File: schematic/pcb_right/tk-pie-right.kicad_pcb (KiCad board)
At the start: 2 copper layers, 150 x 77.5 mm, 35 parts, among them IC1 PCA9539PW,118, J1 NiceView, J2 Battery Connector, U3 SN74LVC1T45DCK

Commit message: Save Ferris
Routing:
- net +5V: track 494.6 -> 490.6 mm, vias 47 -> 45
- net Net-(E3-Pin_1): track 21.5 -> 21.7 mm, vias 0 -> 2
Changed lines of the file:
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@@
 			(xy 96.522284 92.276211) (xy 96.526544 92.29515) (xy 96.531557 92.314169) (xy 96.537324 92.33327)
 			(xy 96.543844 92.35246) (xy 96.55112 92.371739) (xy 96.559148 92.391111) (xy 96.567932 92.410581)
-			(xy 96.587762 92.449827) (xy 96.610607 92.489504) (xy 96.610607 92.489504) (xy 96.628756 92.517845)
-			(xy 96.64862 92.546306) (xy 96.669998 92.574691) (xy 96.692681 92.602813) (xy 96.716468 92.630473)
-			(xy 96.741152 92.657481) (xy 96.766529 92.683644) (xy 96.792395 92.708769) (xy 96.818541 92.732662)
-			(xy 96.844768 92.75513) (xy 96.87087 92.775982) (xy 96.896639 92.795024) (xy 96.921872 92.812061)
-			(xy 96.946366 92.826904) (xy 96.969914 92.839355) (xy 96.992312 92.849226) (xy 97.003643 92.853415)
-			(xy 97.015692 92.857404) (xy 97.028374 92.861183) (xy 97.041608 92.864733) (xy 97.055307 92.868048)
-			(xy 97.06939 92.871107) (xy 97.083773 92.873901) (xy 97.09837 92.876414) (xy 97.113099 92.878634)
-			(xy 97.127877 92.880549) (xy 97.14262 92.882141) (xy 97.157243 92.883401) (xy 97.171663 92.884313)
-			(xy 97.185796 92.884863) (xy 97.199561 92.885041) (xy 97.212869 92.88483) (xy 97.218868 92.88452)
-			(xy 97.225592 92.883953) (xy 97.241046 92.88207) (xy 97.258908 92.879248) (xy 97.278855 92.875549)
-			(xy 97.300562 92.871036) (xy 97.323707 92.865774) (xy 97.347966 92.859825) (xy 97.373015 92.853256)
-			(xy 97.404738 92.844479) (xy 97.43221 92.836397) (xy 97.456496 92.828612) (xy 97.478662 92.820724)
-			(xy 97.49977 92.812333) (xy 97.520886 92.803036) (xy 97.543074 92.792435) (xy 97.567396 92.780129)
-			(xy 97.607879 92.758394) (xy 97.648636 92.734868) (xy 97.689467 92.709687) (xy 97.73018 92.682981)
-			(xy 97.770573 92.654888) (xy 97.810452 92.625538) (xy 97.849618 92.595063) (xy 97.887874 92.5636)
-			(xy 97.912491 92.542576) (xy 97.932105 92.525158) (xy 97.940339 92.517441) (xy 97.947685 92.510198)
-			(xy 97.954263 92.503281) (xy 97.960196 92.49655) (xy 97.965606 92.48986) (xy 97.970611 92.483069)
-			(xy 97.975336 92.476032) (xy 97.979898 92.468608) (xy 97.984422 92.460651) (xy 97.989026 92.452019)
-			(xy 97.998962 92.432156) (xy 98.006663 92.415786) (xy 98.014105 92.398829) (xy 98.021266 92.38137)
-			(xy 98.028123 92.363495) (xy 98.034651 92.345284) (xy 98.040826 92.32683) (xy 98.046625 92.308214)
-			(xy 98.052025 92.289522) (xy 98.057001 92.270839) (xy 98.061531 92.252253) (xy 98.065589 92.233847)
-			(xy 98.069153 92.215705) (xy 98.072198 92.197915) (xy 98.074701 92.180563) (xy 98.07664 92.163732)
-			(xy 98.077989 92.147508) (xy 98.079304 92.125085) (xy 98.079668 92.115331) (xy 98.079789 92.106249)
-			(xy 98.079631 92.097618) (xy 98.079154 92.089211) (xy 98.078327 92.080804) (xy 98.077112 92.072171)
-			(xy 98.07547 92.06309) (xy 98.07337 92.053336) (xy 98.070772 92.042685) (xy 98.06764 92.030911) (xy 98.063938 92.017791)
+			(xy 96.587762 92.449827) (xy 96.610607 92.489504) (xy 96.628756 92.517845) (xy 96.64862 92.546306)
+			(xy 96.669998 92.574691) (xy 96.692681 92.602813) (xy 96.716468 92.630473) (xy 96.741152 92.657481)
+			(xy 96.766529 92.683644) (xy 96.792395 92.708769) (xy 96.818541 92.732662) (xy 96.844768 92.75513)
+			(xy 96.87087 92.775982) (xy 96.896639 92.795024) (xy 96.921872 92.812061) (xy 96.946366 92.826904)
+			(xy 96.969914 92.839355) (xy 96.992312 92.849226) (xy 97.003643 92.853415) (xy 97.015692 92.857404)
+			(xy 97.028374 92.861183) (xy 97.041608 92.864733) (xy 97.055307 92.868048) (xy 97.06939 92.871107)
+			(xy 97.083773 92.873901) (xy 97.09837 92.876414) (xy 97.113099 92.878634) (xy 97.127877 92.880549)
+			(xy 97.14262 92.882141) (xy 97.157243 92.883401) (xy 97.171663 92.884313) (xy 97.185796 92.884863)
+			(xy 97.199561 92.885041) (xy 97.212869 92.88483) (xy 97.218868 92.88452) (xy 97.225592 92.883953)
+			(xy 97.241046 92.88207) (xy 97.258908 92.879248) (xy 97.278855 92.875549) (xy 97.300562 92.871036)
+			(xy 97.323707 92.865774) (xy 97.347966 92.859825) (xy 97.373015 92.853256) (xy 97.404738 92.844479)
+			(xy 97.43221 92.836397) (xy 97.456496 92.828612) (xy 97.478662 92.820724) (xy 97.49977 92.812333)
+			(xy 97.520886 92.803036) (xy 97.543074 92.792435) (xy 97.567396 92.780129) (xy 97.607879 92.758394)
+			(xy 97.648636 92.734868) (xy 97.689467 92.709687) (xy 97.73018 92.682981) (xy 97.770573 92.654888)
+			(xy 97.810452 92.625538) (xy 97.849618 92.595063) (xy 97.887874 92.5636) (xy 97.912491 92.542576)
+			(xy 97.932105 92.525158) (xy 97.940339 92.517441) (xy 97.947685 92.510198) (xy 97.954263 92.503281)
+			(xy 97.960196 92.49655) (xy 97.965606 92.48986) (xy 97.970611 92.483069) (xy 97.975336 92.476032)
+			(xy 97.979898 92.468608) (xy 97.984422 92.460651) (xy 97.989026 92.452019) (xy 97.998962 92.432156)
+			(xy 98.006663 92.415786) (xy 98.014105 92.398829) (xy 98.021266 92.38137) (xy 98.028123 92.363495)
+			(xy 98.034651 92.345284) (xy 98.040826 92.32683) (xy 98.046625 92.308214) (xy 98.052025 92.289522)
+			(xy 98.057001 92.270839) (xy 98.061531 92.252253) (xy 98.065589 92.233847) (xy 98.069153 92.215705)
+			(xy 98.072198 92.197915) (xy 98.074701 92.180563) (xy 98.07664 92.163732) (xy 98.077989 92.147508)
+			(xy 98.079304 92.125085) (xy 98.079668 92.115331) (xy 98.079789 92.106249) (xy 98.079631 92.097618)
+			(xy 98.079154 92.089211) (xy 98.078327 92.080804) (xy 98.077112 92.072171) (xy 98.07547 92.06309)
+			(xy 98.07337 92.053336) (xy 98.070772 92.042685) (xy 98.06764 92.030911) (xy 98.063938 92.017791)
 			(xy 98.05963 92.0031) (xy 98.049056 91.968107) (xy 98.038972 91.935534) (xy 98.030296 91.908836)
 			(xy 98.022526 91.886858) (xy 98.018826 91.877274) (xy 98.015165 91.868434) (xy 98.011483 91.860194)
@@
 	)
 	(segment
-		(start 99.137347 92.962653)
-		(end 100.4 91.7)
-		(width 0.25)
-		(layer "F.Cu")
-		(net 3)
-	)
-	(segment
 		(start 92.312653 85.612653)
 		(end 91 84.3)
@@
 	)
 	(segment
-		(start 99.137347 93.062653)
-		(end 99.137347 92.962653)
-		(width 0.25)
-		(layer "F.Cu")
-		(net 3)
-	)
-	(segment
 		(start 64.187347 41.487347)
 		(end 65.062653 42.362653)
@@
 	)
 	(via
-		(at 100.4 91.7)
-		(size 0.8)
-		(drill 0.4)
-		(layers "F.Cu" "B.Cu")
-		(net 3)
-	)
-	(via
 		(at 80.375 42.4)
 		(size 0.8)
@@
 		(net 3)
 	)
-	(via
-		(at 99.137347 93.062653)
-		(size 0.8)
-		(drill 0.4)
-		(layers "F.Cu" "B.Cu")
-		(net 3)
-	)
 	(segment
 		(start 66.5 42.362653)
@@
 	)
 	(segment
+		(start 99.898905 92.301095)
+		(end 99.898905 92.161095)
+		(width 0.25)
+		(layer "B.Cu")
+		(net 3)
+	)
+	(segment
 		(start 151.0755 83.849)
 		(end 131.7 83.849)
@@
 	)
 	(segment
-		(start 102.9 93.88)
-		(end 101.61781 93.88)
-		(width 0.25)
-		(layer "B.Cu")
-		(net 3)
-	)
-	(segment
 		(start 50.78 58.88)
 		(end 51.45 58.88)
@@
 	)
 	(segment
-		(start 100.4 91.7)
-		(end 102.58 93.88)
-		(width 0.25)
-		(layer "B.Cu")
-		(net 3)
-	)
-	(segment
 		(start 118.475 61)
 		(end 103.5 61)
@@
 	)
 	(segment
+		(start 98.7 93.5)
+		(end 99.898905 92.301095)
+		(width 0.25)
+		(layer "B.Cu")
+		(net 3)
+	)
+	(segment
 		(start 146.45 61.88)
 		(end 142.575 61.88)
@@
 	)
 	(segment
-		(start 101.61781 93.88)
-		(end 100.068905 92.331095)
-		(width 0.25)
-		(layer "B.Cu")
-		(net 3)
-	)
-	(segment
 		(start 29.15 39)
 		(end 29.9 39)
@@
 	)
 	(segment
+		(start 99.898905 92.161095)
+		(end 101.61781 93.88)
+		(width 0.25)
+		(layer "B.Cu")
+		(net 3)
+	)
+	(segment
 		(start 127.45 61.88)
 		(end 125.432306 61.88)
@@
 	)
 	(segment
-		(start 102.58 93.88)
-		(end 102.9 93.88)
-		(width 0.25)
-		(layer "B.Cu")
-		(net 3)
-	)
-	(segment
 		(start 93.350463 85.612653)
 		(end 92.312653 85.612653)
@@
 	)
 	(segment
-		(start 98.7 93.5)
-		(end 99.137347 93.062653)
-		(width 0.25)
-		(layer "B.Cu")
-		(net 3)
-	)
-	(segment
 		(start 146.5 61.3)
 		(end 146.5 61.83)
@@
 	)
 	(segment
-		(start 108.45 93.88)
-		(end 102.9 93.88)
-		(width 0.25)
-		(layer "B.Cu")
-		(net 3)
-	)
-	(segment
 		(start 116.137347 78.725)
 		(end 108.025 78.725)
@@
 	)
 	(segment
+		(start 101.61781 93.88)
+		(end 108.45 93.88)
+		(width 0.25)
+		(layer "B.Cu")
+		(net 3)
+	)
+	(segment
 		(start 63.78 41.38)
 		(end 63.887347 41.487347)
@@
 	)
 	(segment
-		(start 100.068905 92.331095)
+		(start 99.898905 92.161095)
 		(end 93.350463 85.612653)
 		(width 0.25)
@@
 	)
 	(segment
-		(start 98.35 91.25)
-		(end 88.65 91.25)
+		(start 93.93 93.055)
+		(end 95.1 94.225)
+		(width 0.25)
+		(layer "F.Cu")
+		(net 36)
+	)
+	(segment
+		(start 93.93 92.775)
+		(end 93.93 93.055)
+		(width 0.25)
+		(layer "F.Cu")
+		(net 36)
+	)
+	(via
+		(at 93.93 92.775)
+		(size 0.8)
+		(drill 0.4)
+		(layers "F.Cu" "B.Cu")
+		(net 36)
+	)
+	(via
+		(at 95.1 94.225)
+		(size 0.8)
+		(drill 0.4)
+		(layers "F.Cu" "B.Cu")
+		(net 36)
+	)
+	(segment
+		(start 96.255 95.38)
+		(end 108.45 95.38)
+		(width 0.25)
+		(layer "B.Cu")
+		(net 36)
+	)
+	(segment
+		(start 95.1 94.225)
+		(end 96.255 95.38)
 		(width 0.25)
 		(layer "B.Cu")
@@
 	)
 	(segment
-		(start 102.48 95.38)
-		(end 98.35 91.25)
+		(start 88.65 91.25)
+		(end 92.405 91.25)
 		(width 0.25)
 		(layer "B.Cu")
@@
 	)
 	(segment
-		(start 108.45 95.38)
-		(end 102.48 95.38)
+		(start 92.405 91.25)
+		(end 93.93 92.775)
 		(width 0.25)
 		(layer "B.Cu")

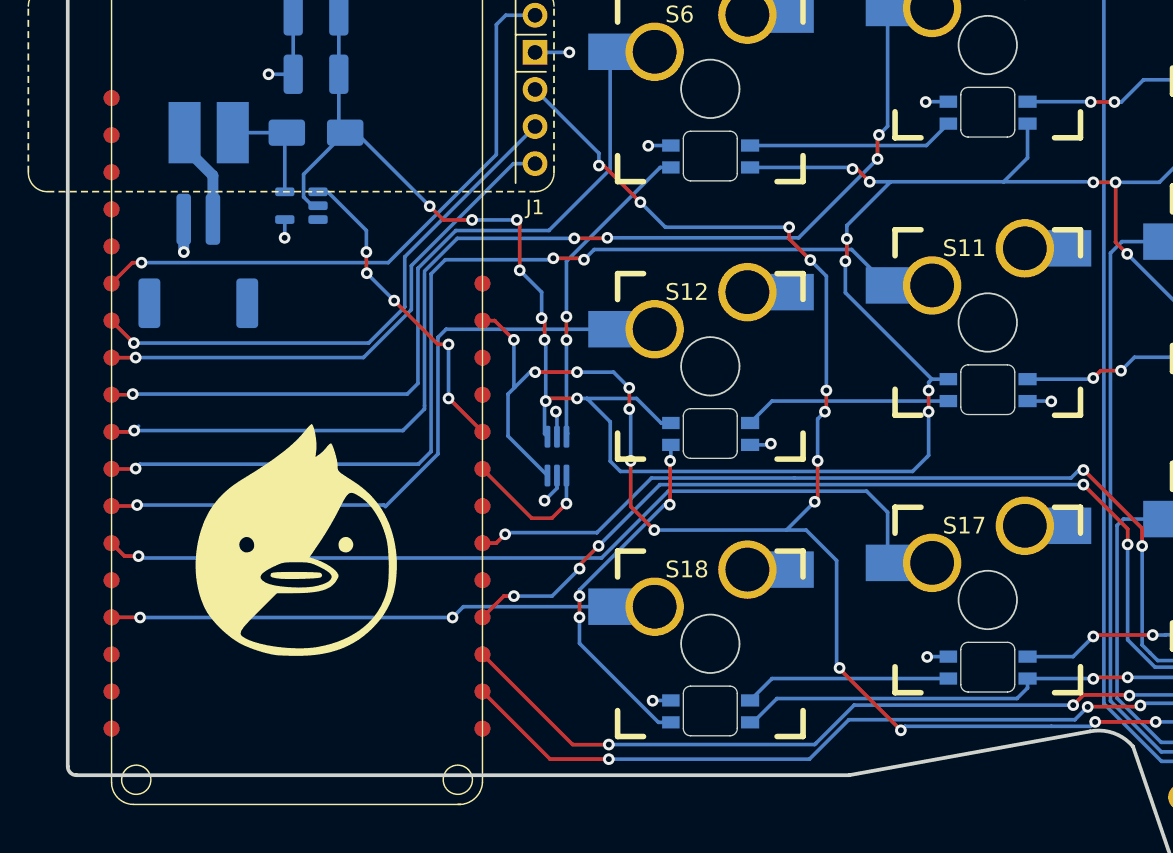
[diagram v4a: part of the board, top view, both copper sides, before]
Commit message: pcb_right: Minor PCB improvments.
- Optimize routing slightly, especially for 3v3 rail.
- Out of caution: Make sure we don't route any wires on the front layer
  where MCU copper will contact the PCB.
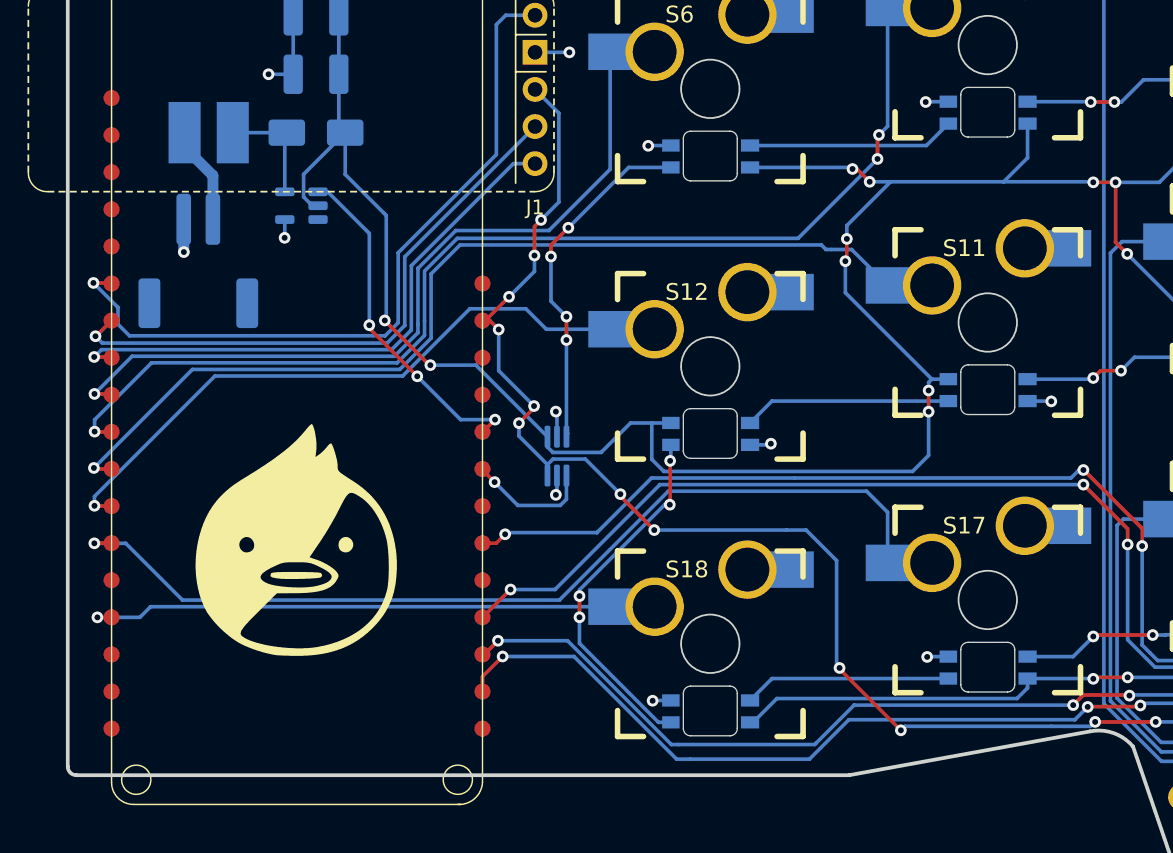
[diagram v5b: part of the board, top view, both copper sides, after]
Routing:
- net +3.3V: track 134.1 -> 98.8 mm, vias 21 -> 14
- net / NV_CS: track 41.8 -> 50.8 mm
- net +5V: track 490.6 -> 485.4 mm, vias 45 -> 39
- net /S17: track 59.5 -> 64.3 mm
- net /NV_MOSI: track 36.3 -> 39.5 mm
- net /NV_SCK: track 37.8 -> 40.8 mm
- net /GPIOE_SCL: track 59.3 -> 61.8 mm
- net /NEOPIXEL_DIN: track 22.1 -> 24.2 mm, vias 2 -> 4
- net /S11: track 67.9 -> 65.9 mm, vias 3 -> 1
- net /S18: track 34.5 -> 36.4 mm, vias 2 -> 1
- net /5V_EN: track 21.9 -> 23.6 mm, vias 5 -> 3
- net /S12: track 43.9 -> 43.0 mm
- net /LED_CTRL: track 9.48 -> 8.62 mm
- net /GPIOE_SDA: track 59.7 -> 60.5 mm
- net GND: track 48.9 -> 48.1 mm
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
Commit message: pcb-right: Add through-holes to vbat pads
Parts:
- moved U1 32.6 mm to (13.2, 25.0)
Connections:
- C4 pad 2: GND -> VBAT-
- C5 pad 1: GND -> VBAT-
- J2 pad 1: /VBAT -> VBAT+
- J2 pad 2: GND -> VBAT-
- L2 pad 1: /VBAT -> VBAT+
- PS1 pad 4: GND -> VBAT-
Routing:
- net VBAT-: track 0.00 -> 55.2 mm
- net VBAT+: track 0.00 -> 29.2 mm, vias 0 -> 2
- net GND: track 48.1 -> 38.7 mm, vias 28 -> 25
- net /VBAT: track 6.73 -> 0.00 mm
